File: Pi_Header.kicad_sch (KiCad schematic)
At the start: 31 parts, among them J1 Raspberry_Pi_2_3, J2 UART, J3 I2C, J4 Power_IN, U1 BD9F800MUX-ZE2

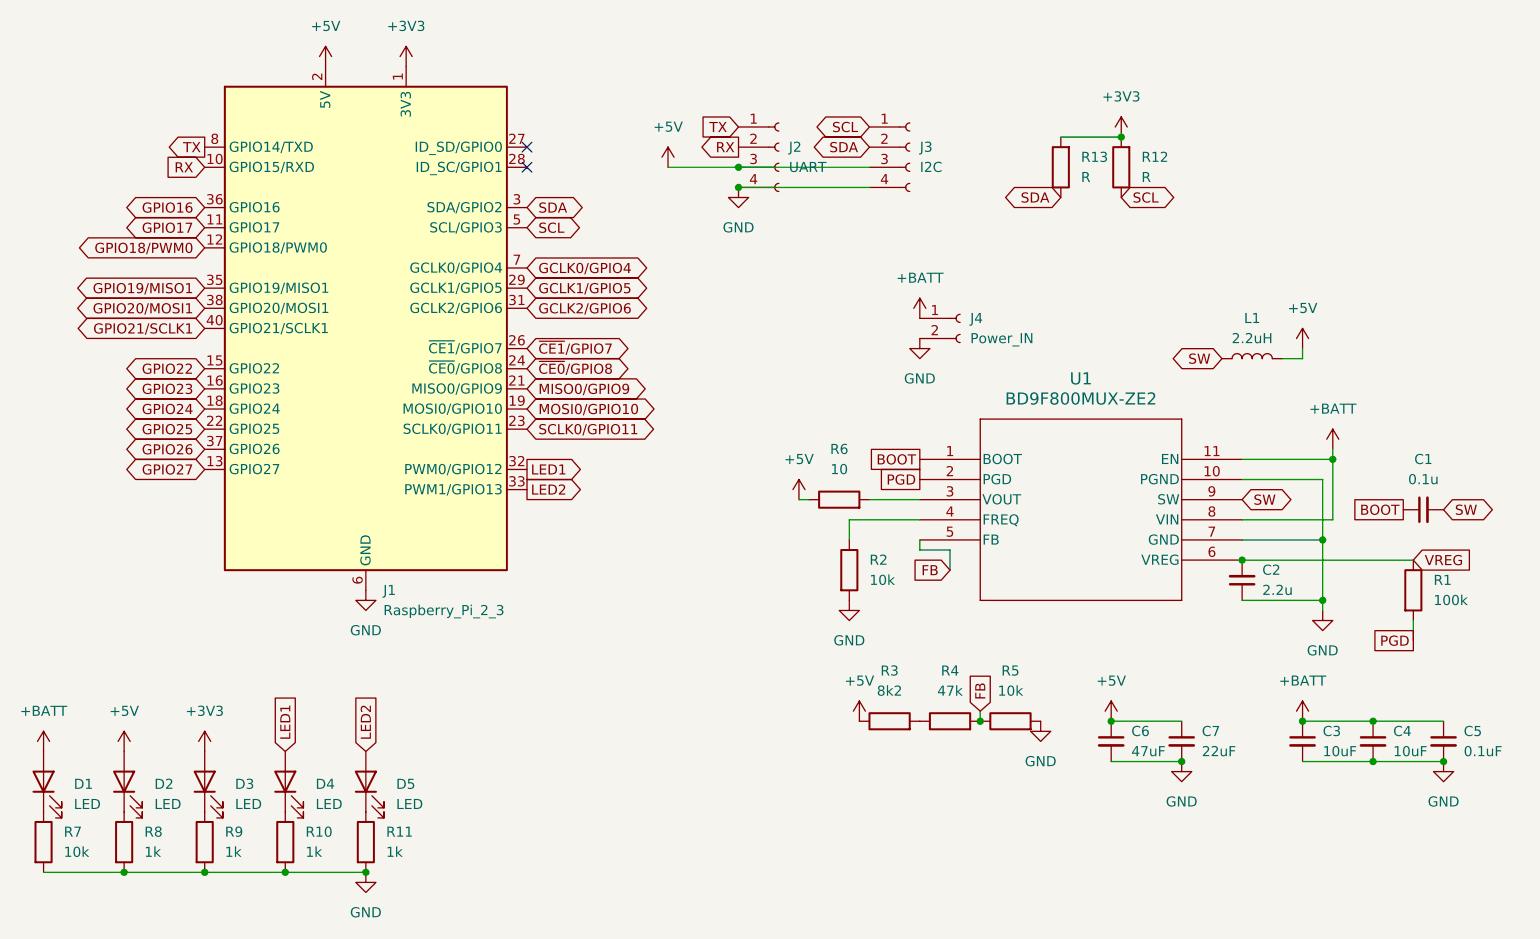
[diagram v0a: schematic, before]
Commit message: 電源回り諸定数の修正、参照先の追加
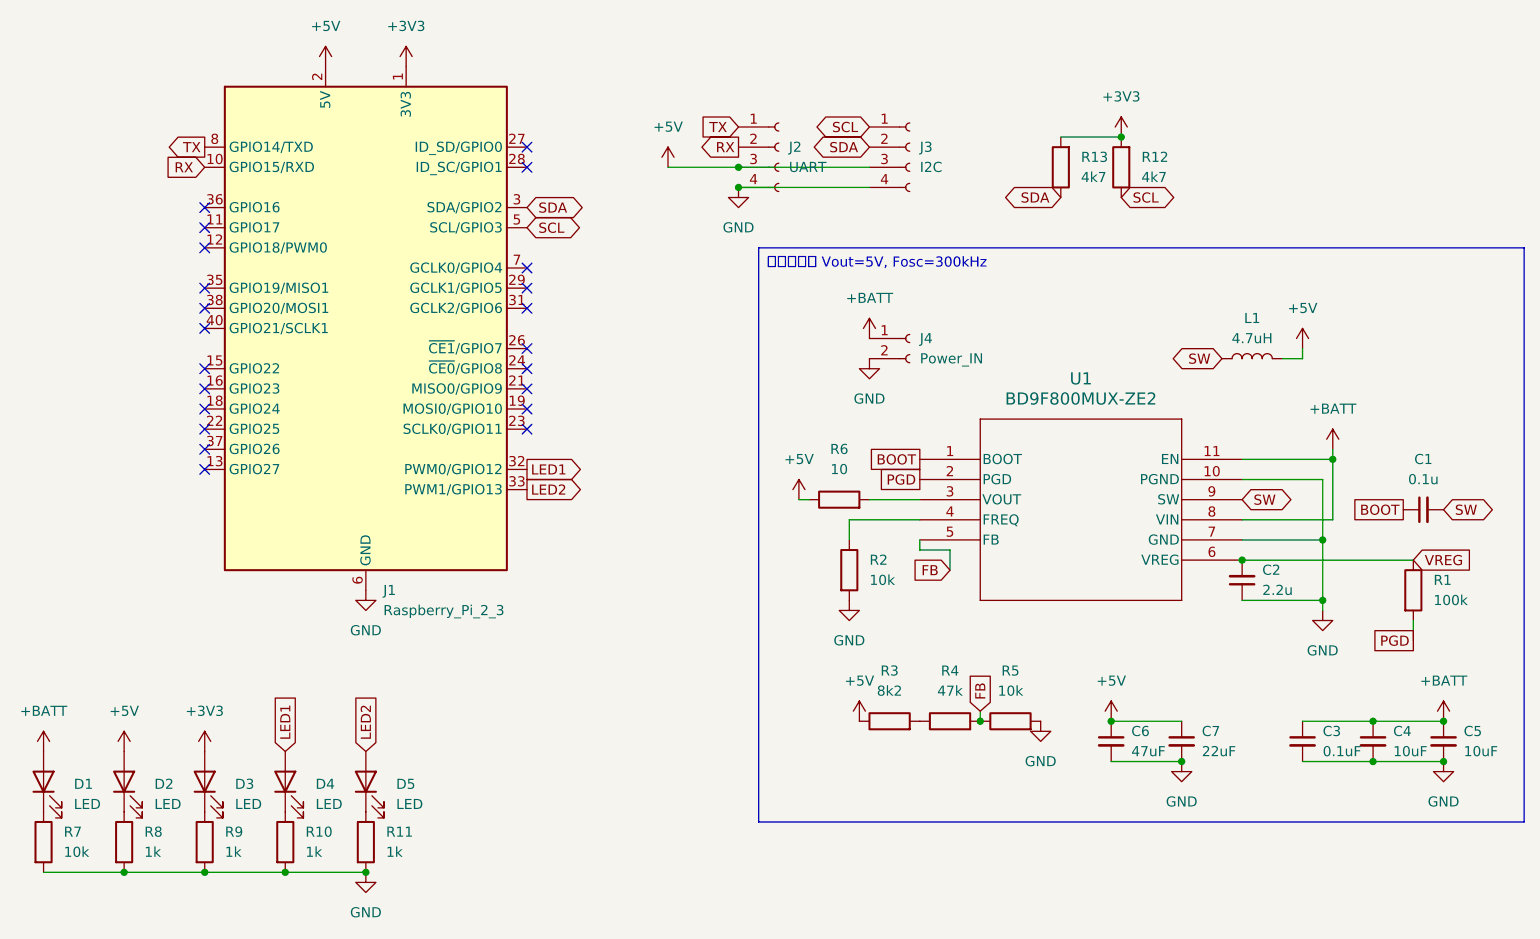
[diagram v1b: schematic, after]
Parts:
- L1: value 2.2uH -> 4.7uH
- R12, R13: value R -> 4k7
- renumbered C5 to C3, C3 to C5
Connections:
- net GCLK0/GPIO4: no longer names the net of J1.7 (GCLK0/GPIO4)
- net GCLK1/GPIO5: no longer names the net of J1.29 (GCLK1/GPIO5)
- net GCLK2/GPIO6: no longer names the net of J1.31 (GCLK2/GPIO6)
- net GPIO16: no longer names the net of J1.36 (GPIO16)
- net GPIO17: no longer names the net of J1.11 (GPIO17)
- net GPIO18/PWM0: no longer names the net of J1.12 (GPIO18/PWM0)
- net GPIO19/MISO1: no longer names the net of J1.35 (GPIO19/MISO1)
- net GPIO20/MOSI1: no longer names the net of J1.38 (GPIO20/MOSI1)
- net GPIO21/SCLK1: no longer names the net of J1.40 (GPIO21/SCLK1)
- net GPIO22: no longer names the net of J1.15 (GPIO22)
- net GPIO23: no longer names the net of J1.16 (GPIO23)
- net GPIO24: no longer names the net of J1.18 (GPIO24)
- net GPIO25: no longer names the net of J1.22 (GPIO25)
- net GPIO26: no longer names the net of J1.37 (GPIO26)
- net GPIO27: no longer names the net of J1.13 (GPIO27)
- net MISO0/GPIO9: no longer names the net of J1.21 (MISO0/GPIO9)
- net MOSI0/GPIO10: no longer names the net of J1.19 (MOSI0/GPIO10)
- net SCLK0/GPIO11: no longer names the net of J1.23 (SCLK0/GPIO11)
- net ~{CE0}/GPIO8: no longer names the net of J1.24 (~{CE0}/GPIO8)
- net ~{CE1}/GPIO7: no longer names the net of J1.26 (~{CE1}/GPIO7)
- no-connect marks 2 -> 22
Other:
- moved on the sheet: C3, C5, J4
